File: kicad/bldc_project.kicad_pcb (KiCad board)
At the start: 4 copper layers, 115 x 60 mm, 156 parts, among them J1 Conn_ARM_SWD_TagConnect_TC203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, J2 Screw_Terminal_01x03, J3 Screw_Terminal_01x03, J4 TYPE-C-31-M-12, Q1 IRFZ44N, Q2 IRFZ44N, Q3 IRFZ44N, Q4 IRFZ44N, Q5 IRFZ44N, Q6 IRFZ44N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

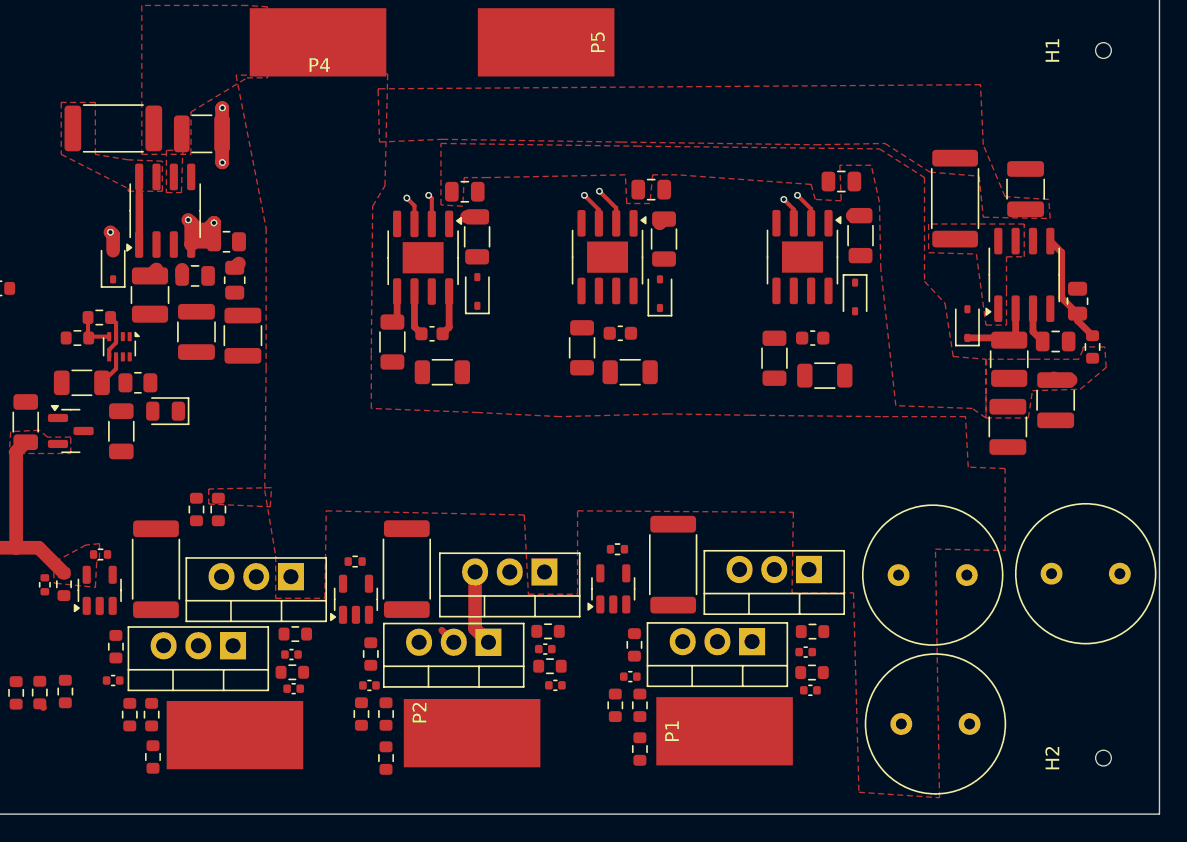
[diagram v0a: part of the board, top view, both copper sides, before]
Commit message: minor 10 V power plane changes + phase planes poured
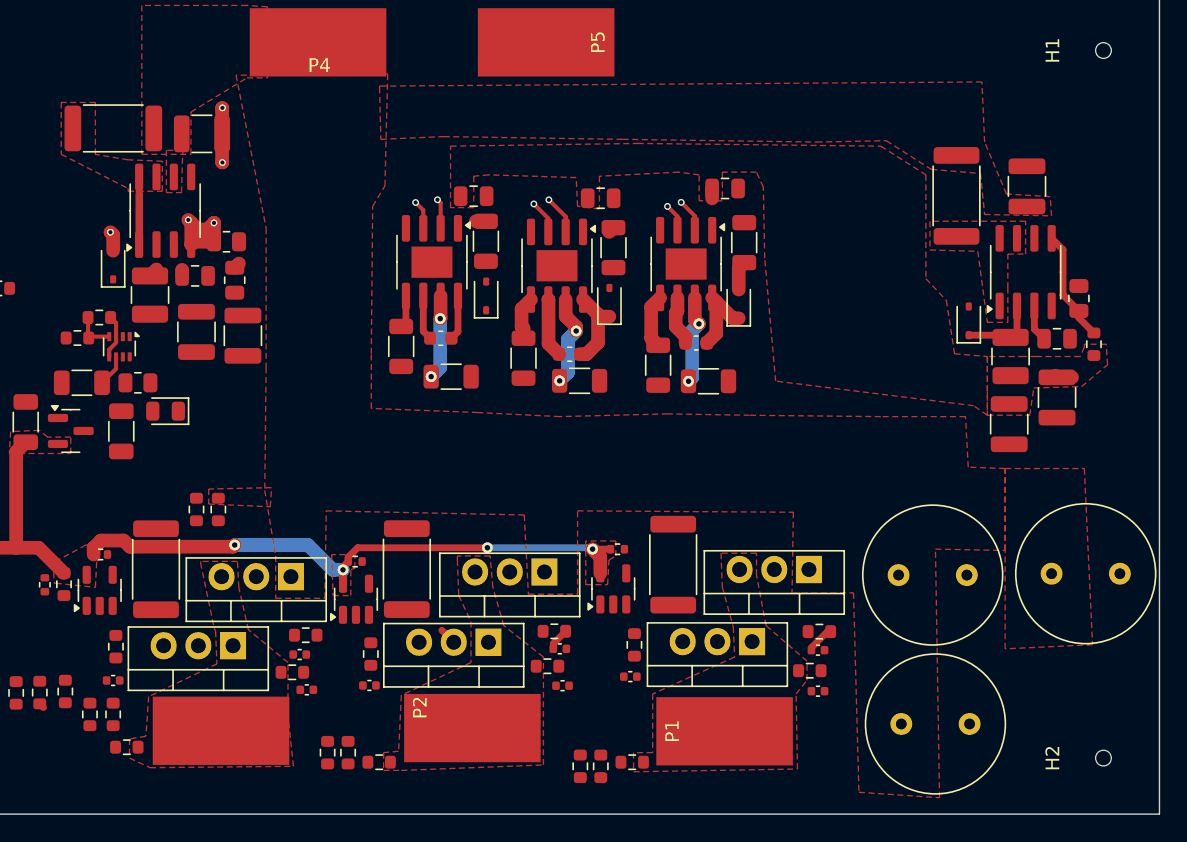
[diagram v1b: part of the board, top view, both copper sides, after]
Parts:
- moved C4 8.54 mm to (119.3, 106.0)
- moved R5 8.53 mm to (116.5, 107.6)
- moved U1 8.53 mm to (118.5, 100.2)
- moved R1 8.53 mm to (122.8, 98.7)
- moved C1 8.53 mm to (121.4, 94.7)
- moved D1 8.53 mm to (122.4, 103.2), turned to 90 degrees
- moved R4 8.52 mm to (120.2, 108.8)
- moved R29 5.30 mm to (112.3, 137.0), turned to 90 degrees
- moved R30 5.15 mm to (110.8, 137.0), turned to -90 degrees
- moved R9 4.35 mm to (106.6, 107.1)
- moved C5 4.01 mm to (110.0, 106.8)
- moved R26 3.96 mm to (93.8, 136.0), turned to 90 degrees
- moved R27 3.76 mm to (92.3, 136.0), turned to -90 degrees
- moved U2 3.75 mm to (109.1, 100.4)
- moved R2 3.75 mm to (113.2, 99.0)
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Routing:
- net +3.3V: track 65.6 -> 109.3 mm, vias 0 -> 4
- net Net-(U2-HO): track 0.00 -> 6.77 mm, vias 0 -> 2
- net Net-(U1-HO): track 0.00 -> 6.55 mm, vias 0 -> 2
- net Net-(U3-HO): track 0.37 -> 6.57 mm, vias 0 -> 2
- net Net-(D2-K): track 0.00 -> 6.09 mm
- net Net-(D1-K): track 0.00 -> 5.86 mm
- net /DRIVER/PhaseV: track 5.55 -> 0.00 mm
- net Net-(U2-VS): track 0.00 -> 4.33 mm
- net Net-(U1-LO): track 0.00 -> 3.96 mm
- net Net-(U1-VS): track 0.00 -> 3.66 mm
- net Net-(U2-LO): track 0.00 -> 3.18 mm
- net Net-(D1-A): track 0.00 -> 2.14 mm
- net Net-(C13-Pad1): track 0.00 -> 2.08 mm
- net Net-(C14-Pad1): track 0.00 -> 1.66 mm
- added copper zone on F.Cu, net /DRIVER/PhaseU
- added copper zone on F.Cu, net /DRIVER/PhaseV
- added copper zone on F.Cu, net /DRIVER/PhaseW

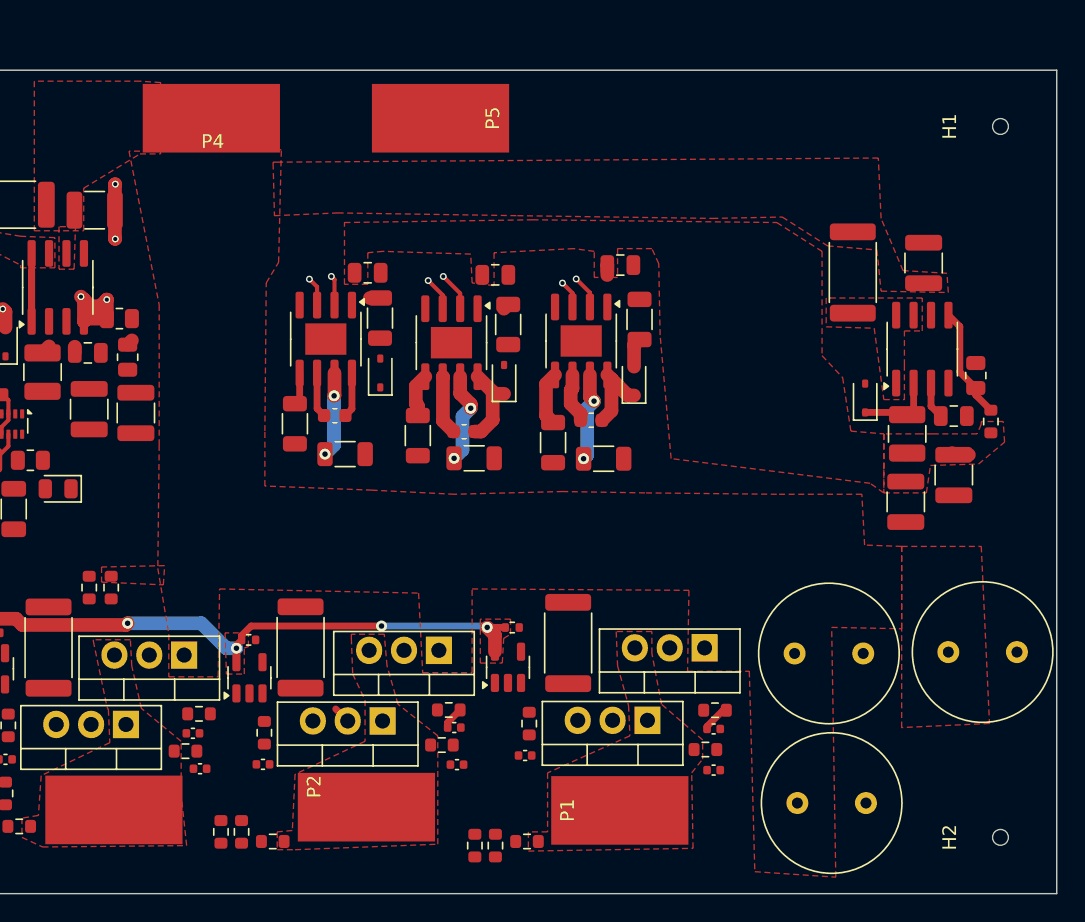
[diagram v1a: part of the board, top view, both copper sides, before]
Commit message: [kicad] Routing bootstraps [cubemx] TODO: check feasibility of adc-signal switch on cpu
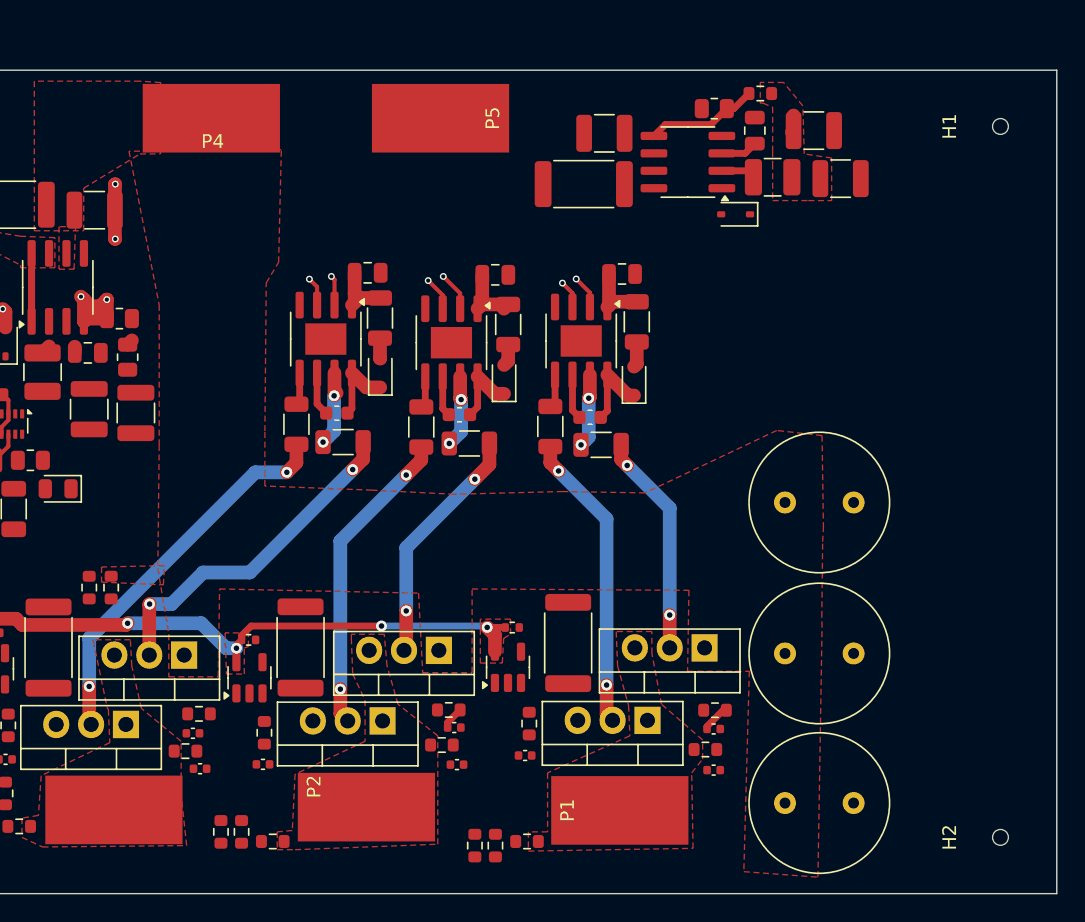
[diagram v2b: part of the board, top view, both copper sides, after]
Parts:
- moved R48 29.2 mm to (131.6, 82.2), turned to 0 degrees
- moved R55 27.2 mm to (128.2, 83.3), turned to 180 degrees
- moved C39 27.1 mm to (135.5, 84.9), turned to 180 degrees
- moved C43 25.4 mm to (131.2, 84.9), turned to -90 degrees
- moved C45 25.1 mm to (120.2, 85.1), turned to 180 degrees
- moved C41 24.0 mm to (137.4, 88.4), turned to 0 degrees
- moved U11 21.9 mm to (126.3, 87.2), turned to 180 degrees
- moved L2 21.1 mm to (132.5, 88.3), turned to 180 degrees
- moved R60 20.6 mm to (118.7, 88.8), turned to 0 degrees
- moved D8 16.4 mm to (129.8, 91.0), turned to 180 degrees
- moved C16 16.1 mm to (133.4, 112.0)
- moved C5 1.28 mm to (109.7, 105.6)
- moved R5 1.19 mm to (116.3, 106.5)
- moved R8 1.14 mm to (110.4, 107.7)
- moved R4 1.03 mm to (120.0, 107.8)
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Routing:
- net Net-(Q6-G): track 0.00 -> 28.1 mm, vias 0 -> 2
- net Net-(Q5-G): track 0.00 -> 24.9 mm, vias 0 -> 2
- net Net-(Q2-G): track 0.00 -> 21.8 mm, vias 0 -> 2
- net Net-(Q4-G): track 1.24 -> 22.6 mm, vias 0 -> 2
- net Net-(Q3-G): track 0.00 -> 17.7 mm, vias 0 -> 2
- net Net-(Q1-G): track 0.00 -> 16.3 mm, vias 0 -> 2
- net +10V: track 3.33 -> 15.2 mm
- net Net-(D8-K): track 5.62 -> 2.72 mm
- net Net-(D3-K): track 3.29 -> 5.55 mm
- net Net-(D2-A): track 0.00 -> 1.61 mm
- net Net-(U1-LO): track 3.96 -> 2.44 mm
- net Net-(U2-HO): track 6.77 -> 5.26 mm
- net Net-(D3-A): track 0.00 -> 1.49 mm
- net Net-(U2-VS): track 4.33 -> 2.95 mm
- net Net-(U3-HO): track 6.57 -> 5.38 mm
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- removed copper zone on F.Cu, net /POWER/VBUCK10_IN

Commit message: [kicad] Changed CPU adc / pwm inputs to facilitate routing
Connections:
- U7 pad 11: /CPU/MEAS_TEMP -> Phase_GVIRTUAL
- U7 pad 12: /CPU/MEAS_BAT -> PhaseU_DIV
- U7 pad 15: PhaseU_DIV -> PhaseV_DIV
- U7 pad 16: PhaseV_DIV -> PhaseW_DIV
- U7 pad 17: PhaseV_SWITCH -> PhaseU_SWITCH
- U7 pad 18: PhaseU_SWITCH -> PhaseU_SD
- U7 pad 19: PhaseU_SD -> PhaseV_SWITCH
- U7 pad 20: PhaseW_DIV -> PhaseW_CURRENT
- U7 pad 25: PhaseW_CURRENT -> PhaseV_CURRENT
- U7 pad 26: Phase_GVIRTUAL -> PhaseU_CURRENT
- U7 pad 27: PhaseV_CURRENT -> /CPU/MEAS_BAT
- U7 pad 28: PhaseU_CURRENT -> /CPU/MEAS_TEMP
- U7 pad 40: PhaseV_SD -> PhaseW_SD
- U7 pad 42: PhaseW_SD -> PhaseV_SD
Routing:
- net Phase_GVIRTUAL: track 0.00 -> 3.11 mm, vias 0 -> 1
- net /CPU/MEAS_TEMP: track 3.11 -> 0.00 mm, vias 1 -> 0
- net /CPU/MEAS_BAT: track 2.88 -> 0.00 mm, vias 1 -> 0
- net PhaseW_DIV: track 1.93 -> 4.80 mm
- net PhaseU_DIV: track 4.90 -> 2.88 mm
- net PhaseW_CURRENT: track 0.00 -> 1.93 mm, vias 0 -> 1
- net PhaseU_SWITCH: track 5.23 -> 6.19 mm
- net PhaseV_SWITCH: track 6.60 -> 5.83 mm

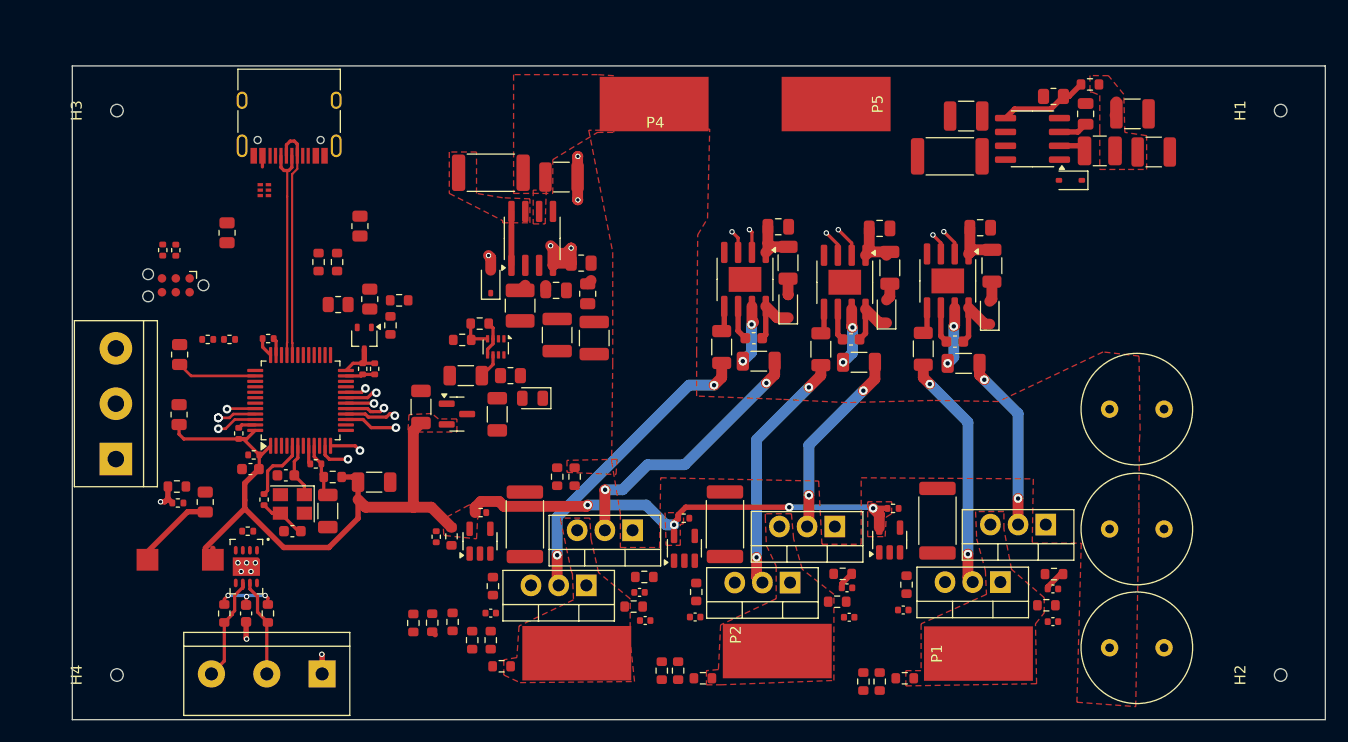
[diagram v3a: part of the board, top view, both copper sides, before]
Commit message: Rough routing finished, checks next
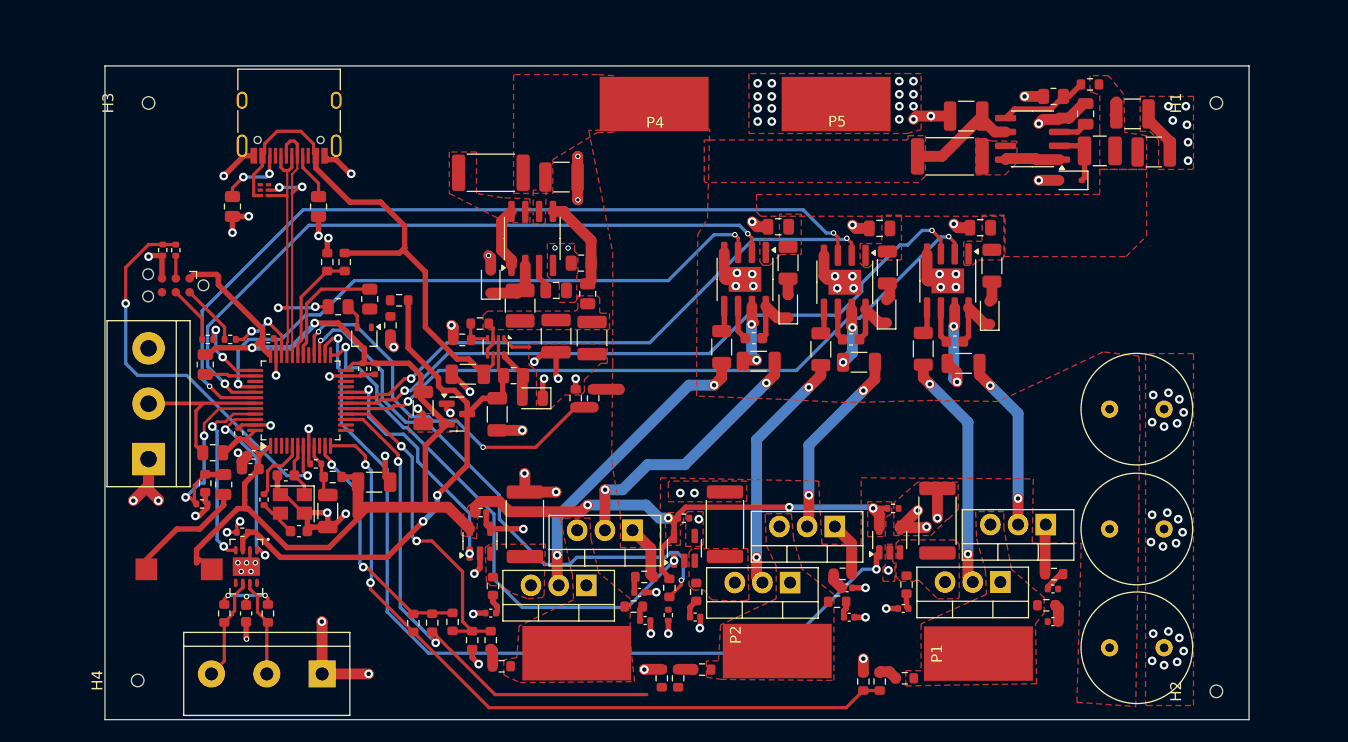
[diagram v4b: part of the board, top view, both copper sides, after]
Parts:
- moved TH1 22.5 mm to (92.9, 130.9), turned to -90 degrees
- moved R38 20.6 mm to (93.0, 128.4)
- moved R34 7.40 mm to (86.0, 111.0)
- moved R35 7.40 mm to (84.4, 111.0)
- moved H2 6.09 mm to (143.2, 137.9)
- moved H1 5.94 mm to (143.2, 83.9)
- moved R46 4.67 mm to (51.1, 116.0), turned to 180 degrees
- moved R58 4.20 mm to (60.8, 93.4), turned to 90 degrees
- moved J3 3.00 mm to (45.2, 116.6)
- moved H3 2.98 mm to (45.2, 83.9)
- moved R37 2.62 mm to (50.4, 118.8), turned to -90 degrees
- moved R44 2.52 mm to (50.4, 107.9)
- moved R56 2.46 mm to (52.9, 93.4), turned to 90 degrees
- moved R49 2.40 mm to (63.2, 98.5)
- moved R36 2.34 mm to (52.1, 118.9)
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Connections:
- U7 pad 27: /CPU/MEAS_BAT -> /CPU/MEAS_TEMP
- U7 pad 28: /CPU/MEAS_TEMP -> /CPU/MEAS_BAT
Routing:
- net GND: track 27.6 -> 166.0 mm, vias 13 -> 127
- net PhaseU_CURRENT: track 0.00 -> 80.7 mm, vias 0 -> 2
- net PhaseV_SD: track 2.49 -> 76.7 mm, vias 1 -> 2
- net PhaseU_DIV: track 2.88 -> 68.0 mm, vias 1 -> 2
- net PhaseW_SWITCH: track 2.19 -> 64.7 mm, vias 1 -> 2
- net PhaseU_SD: track 4.82 -> 63.3 mm
- net PhaseU_SWITCH: track 6.19 -> 63.7 mm
- net PhaseW_SD: track 2.12 -> 56.5 mm, vias 1 -> 2
- net +5V: track 0.00 -> 54.3 mm, vias 0 -> 2
- net /CPU/MEAS_TEMP: track 0.00 -> 51.5 mm, vias 0 -> 2
- net +3.3V: track 109.3 -> 158.9 mm, vias 4 -> 6
- net PhaseV_CURRENT: track 0.00 -> 48.9 mm, vias 0 -> 2
- net PhaseV_SWITCH: track 5.83 -> 53.8 mm
- net USB_VBUS: track 3.35 -> 49.1 mm
- net PhaseV_DIV: track 5.29 -> 48.5 mm, vias 1 -> 2
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- added copper zone on F.Cu, net /DRIVER/PhaseU_CURRENT+
- added copper zone on F.Cu, net /DRIVER/PhaseV_CURRENT+
- added copper zone on F.Cu, net /DRIVER/PhaseW_CURRENT+
- added copper zone on F.Cu, net /POWER/VBUCK10_IN
- added copper zone on F.Cu, net /POWER/VBUCK5_OUT
- added copper zone on F.Cu, net GND
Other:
- board size 115 x 60 mm -> 105 x 60 mm
